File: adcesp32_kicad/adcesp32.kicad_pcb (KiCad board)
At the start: 2 copper layers, 35 x 66 mm, 38 parts, among them IC1 PCM1862DBT, J2 USB_C_Receptacle_USB2.0_16P, J3 RCJ-2112, J4 Conn_01x05_Pin, J5 Conn_01x05_Pin, J6 Conn_01x04_Pin, J7 Conn_01x04_Pin, J8 Conn_01x04_Pin, J9 SJ-43514, U1 ESP32-S3-WROOM-1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

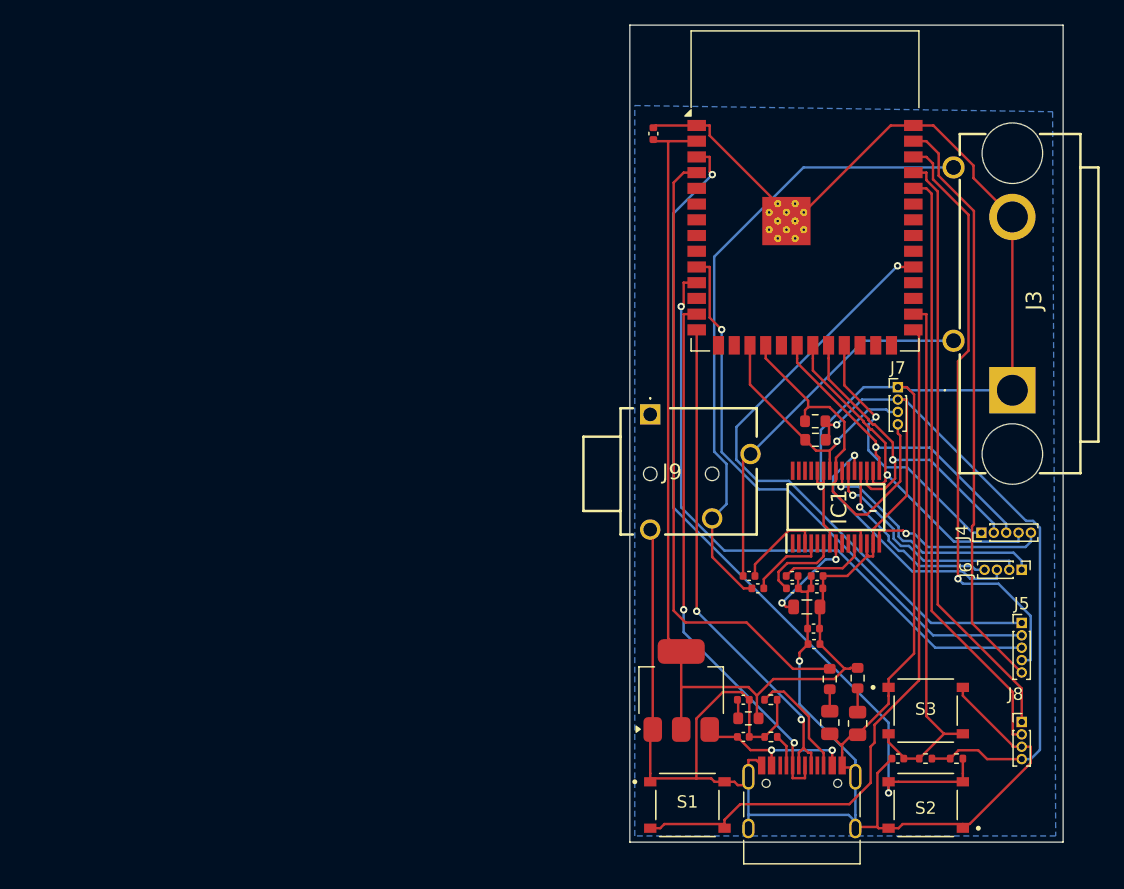
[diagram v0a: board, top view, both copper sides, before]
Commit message: completed 52x52 pcb design
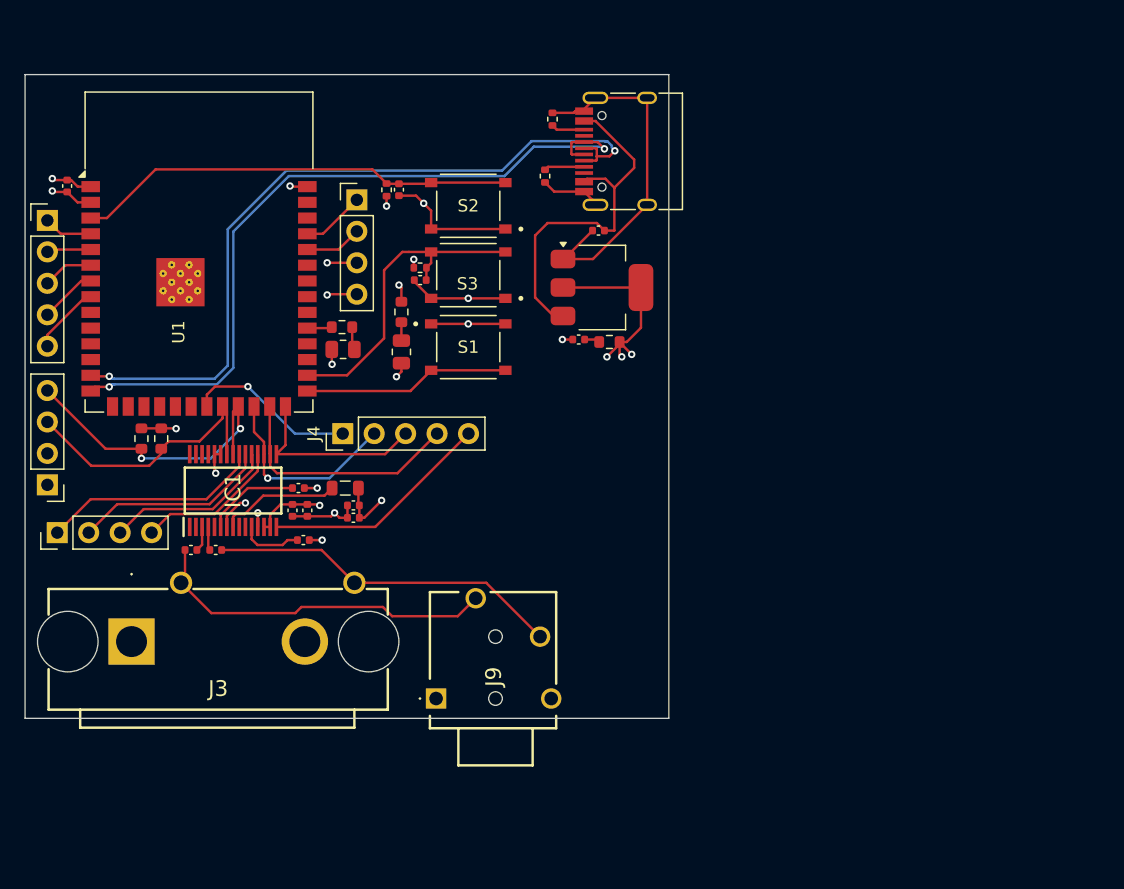
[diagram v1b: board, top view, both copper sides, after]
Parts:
- added C13: 10uF, Capacitor_SMD:C_0402_1005Metric, F.Cu at (181.2, 68.3)
- J4, J5: footprint Connector_PinHeader_1.00mm:PinHeader_1x05_P1.00mm_Vertical -> Connector_PinHeader_2.54mm:PinHeader_1x05_P2.54mm_Vertical
- J6, J7, J8: footprint Connector_PinHeader_1.00mm:PinHeader_1x04_P1.00mm_Vertical -> Connector_PinHeader_2.54mm:PinHeader_1x04_P2.54mm_Vertical
- moved J5 85.2 mm to (152.8, 70.8)
- moved J6 78.0 mm to (153.6, 96.0), turned to 90 degrees
- moved J3 74.0 mm to (159.6, 104.8), turned to 180 degrees
- moved J7 69.2 mm to (152.8, 92.1), turned to 180 degrees
- moved J8 68.3 mm to (177.8, 69.1)
- moved R1 65.0 mm to (180.2, 68.3), turned to -90 degrees
- moved S2 60.9 mm to (186.8, 69.6)
- moved R9 56.9 mm to (182.9, 74.6), turned to 180 degrees
- moved J2 55.3 mm to (200.2, 65.2), turned to 90 degrees
- moved C12 54.6 mm to (182.9, 75.6)
- moved R3 54.4 mm to (160.4, 88.4), turned to -90 degrees
- moved R2 52.8 mm to (162.0, 88.4), turned to -90 degrees
- moved J4 52.2 mm to (176.7, 88.0)
- moved S3 51.0 mm to (186.8, 75.2), turned to 180 degrees
- moved R5 50.1 mm to (193.6, 62.6), turned to 90 degrees
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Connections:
- J5 pad 1: ESP_GPIO38 -> ESP_IO4
- J5 pad 2: ESP_GPIO17 -> ESP_IO5
- J5 pad 3: ESP_GPIO18 -> ESP_IO6
- J5 pad 4: ESP_GPIO2 -> ESP_IO7
- J5 pad 5: ESP_GPIO1 -> ESP_IO15
- R6 pad 2: ESP_GPIO4 -> ESP_IO38
- U1 pad 10: ESP_GPIO17 -> unconnected-(U1-IO17-Pad10)
- U1 pad 11: ESP_GPIO18 -> unconnected-(U1-IO18-Pad11)
- U1 pad 17: SCL -> unconnected-(U1-IO9-Pad17)
- U1 pad 18: SDA -> unconnected-(U1-IO10-Pad18)
- U1 pad 20: LRCK -> unconnected-(U1-IO12-Pad20)
- U1 pad 21: BCK -> I2S_DOUT
- U1 pad 22: DOUT_ADC -> SCL
- U1 pad 23: I2S_DOUT -> SDA
- U1 pad 24: unconnected-(U1-IO47-Pad24) -> DOUT_ADC
- U1 pad 25: unconnected-(U1-IO48-Pad25) -> BCK
- U1 pad 26: unconnected-(U1-IO45-Pad26) -> LRCK
- U1 pad 31: ESP_GPIO38 -> ESP_IO38
- U1 pad 38: ESP_GPIO2 -> unconnected-(U1-IO2-Pad38)
- U1 pad 39: ESP_GPIO1 -> unconnected-(U1-IO1-Pad39)
- U1 pad 4: ESP_GPIO4 -> ESP_IO4
- U1 pad 5: unconnected-(U1-IO5-Pad5) -> ESP_IO5
- U1 pad 6: unconnected-(U1-IO6-Pad6) -> ESP_IO6
- U1 pad 7: unconnected-(U1-IO7-Pad7) -> ESP_IO7
- U1 pad 8: unconnected-(U1-IO15-Pad8) -> ESP_IO15
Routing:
- net GND: track 251.4 -> 83.3 mm, vias 2 -> 15
- net +3V3: track 149.2 -> 39.1 mm, vias 1 -> 11
- net ESP_GPIO18: track 51.5 -> 0.00 mm, vias 1 -> 0
- net ESP_GPIO4: track 51.3 -> 0.00 mm
- net ESP_GPIO38: track 50.9 -> 0.00 mm, vias 1 -> 0
- net ESP_GPIO2: track 48.3 -> 0.00 mm, vias 1 -> 0
- net ESP_GPIO1: track 47.3 -> 0.00 mm
- net ESP_GPIO17: track 46.8 -> 0.00 mm, vias 1 -> 0
- net RX: track 48.8 -> 4.61 mm
- net TX: track 48.6 -> 5.13 mm
- net BOOT: track 58.3 -> 16.7 mm
- net RST: track 69.8 -> 35.7 mm, vias 2 -> 0
- net R1: track 51.7 -> 28.6 mm
- net USB_D+: track 40.7 -> 61.1 mm
- net PHYS_INT: track 43.7 -> 25.8 mm
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- added copper zone on In2.Cu, net +3V3
- added copper zone on In1.Cu, net GND
- removed copper zone on B.Cu, net GND
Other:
- board size 35 x 66 mm -> 52 x 52 mm
- copper layers 2 -> 4
- board text removed: "J8"
